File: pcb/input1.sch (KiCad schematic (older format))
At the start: 32 parts, among them Q1 BC847, Q2 BC847, U10 SN74LVCC4245APW, U11 SN74LVCC4245APW, U14 SN74LVCC4245APW, U18 SN74LVCC4245APW, U19 SN74LVCC4245APW, U20 SN74LVC2G17, U4 PCEngineExpansion, U9 SN74LVCC4245APW

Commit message: New layout checkpoint
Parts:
- Q1, Q2: symbol Transistor_BJT:BC847 -> pcehd-rescue:BC847-Transistor_BJT
- R22, R23, R24, R25, R26, R27, R28, R29, R30: symbol Device:R_Small -> pcehd-rescue:R_Small-Device
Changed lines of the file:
@@
 EESchema Schematic File Version 4
-LIBS:pcehd-cache
 EELAYER 30 0
 EELAYER END
@@
 CS_O
 $Comp
-L Device:R_Small R28
+L pcehd-rescue:R_Small-Device R28
 U 1 1 5E20B4F6
 P 2600 6150
@@
 	2700 5950 2700 5500
 $Comp
-L Device:R_Small R27
+L pcehd-rescue:R_Small-Device R27
 U 1 1 5E220BE1
 P 2600 4050
@@
 	2700 2050 2600 2050
 $Comp
-L Device:R_Small R22
+L pcehd-rescue:R_Small-Device R22
 U 1 1 5E4396BE
 P 2600 1950
@@
 $EndComp
 $Comp
-L Device:R_Small R26
+L pcehd-rescue:R_Small-Device R26
 U 1 1 5E1D0EB3
 P 6450 1250
@@
 $EndComp
 $Comp
-L Device:R_Small R29
+L pcehd-rescue:R_Small-Device R29
 U 1 1 610BFA1D
 P 6400 3450
@@
 	10000 5950 10350 5950
 $Comp
-L Transistor_BJT:BC847 Q1
+L pcehd-rescue:BC847-Transistor_BJT Q1
 U 1 1 5F31D333
 P 10250 6200
@@
 $EndComp
 $Comp
-L Device:R_Small R23
+L pcehd-rescue:R_Small-Device R23
 U 1 1 5F31D320
 P 9650 6200
@@
 $EndComp
 $Comp
-L Device:R_Small R30
+L pcehd-rescue:R_Small-Device R30
 U 1 1 5F31D31A
 P 9800 6350
@@
 	9950 4850 10300 4850
 $Comp
-L Transistor_BJT:BC847 Q2
+L pcehd-rescue:BC847-Transistor_BJT Q2
 U 1 1 60FF82DE
 P 10200 5100
@@
 $EndComp
 $Comp
-L Device:R_Small R24
+L pcehd-rescue:R_Small-Device R24
 U 1 1 60C571BE
 P 9600 5100
@@
 $EndComp
 $Comp
-L Device:R_Small R25
+L pcehd-rescue:R_Small-Device R25
 U 1 1 60C54728
 P 9750 5250

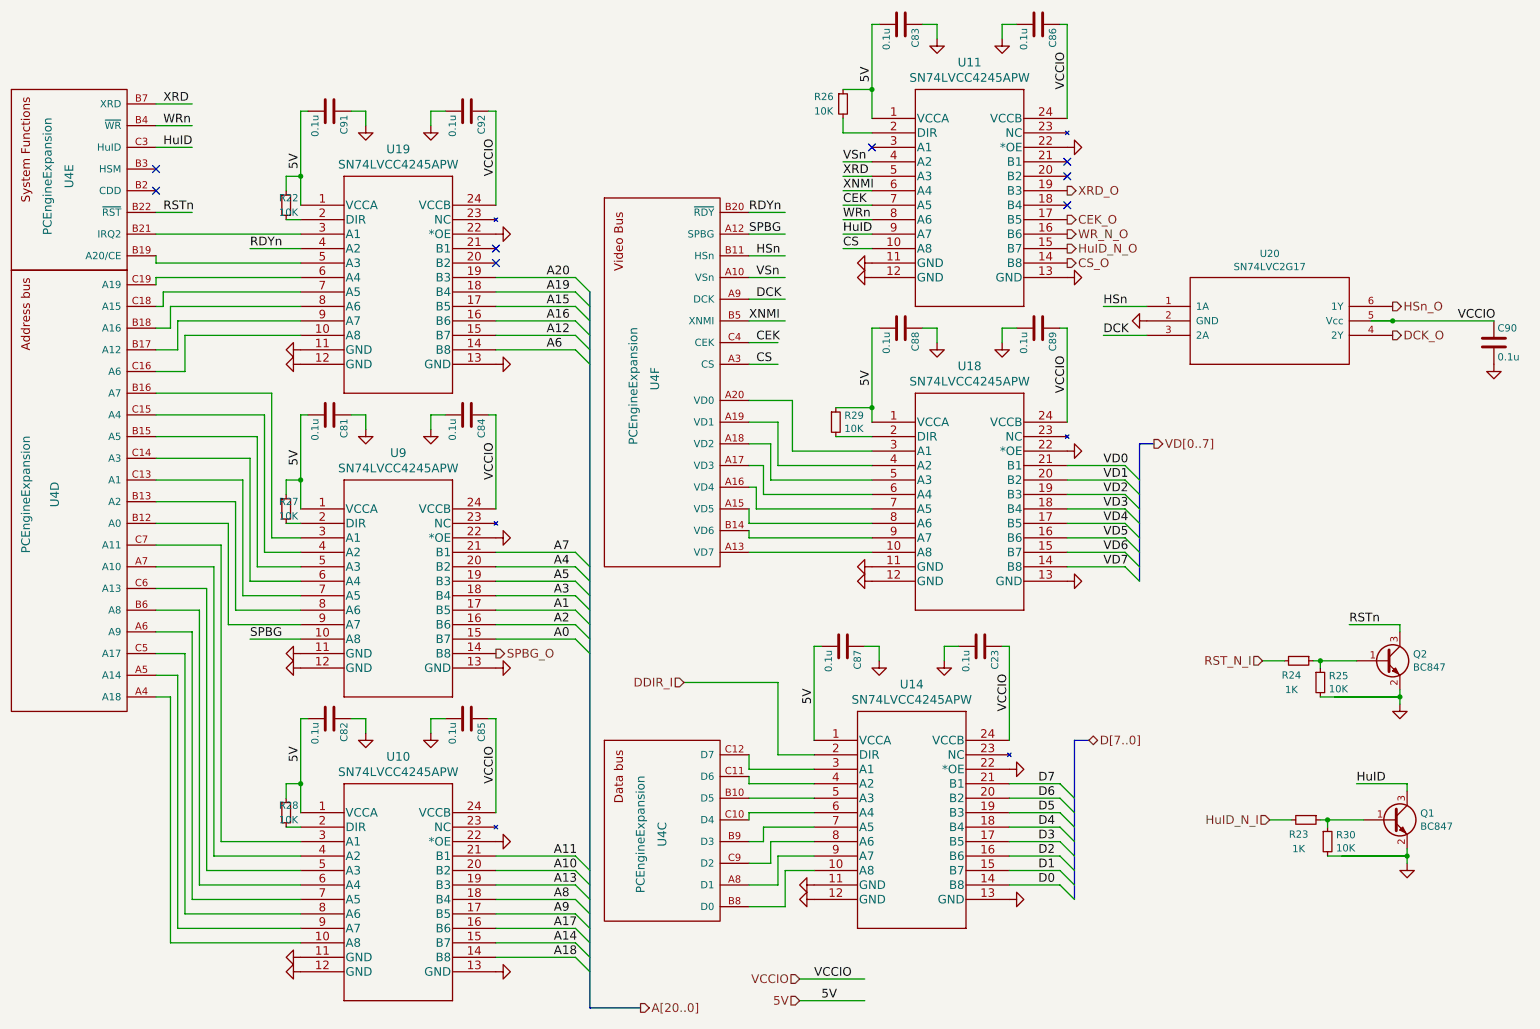
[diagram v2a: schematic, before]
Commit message: Added CDD signal to last open IO pin
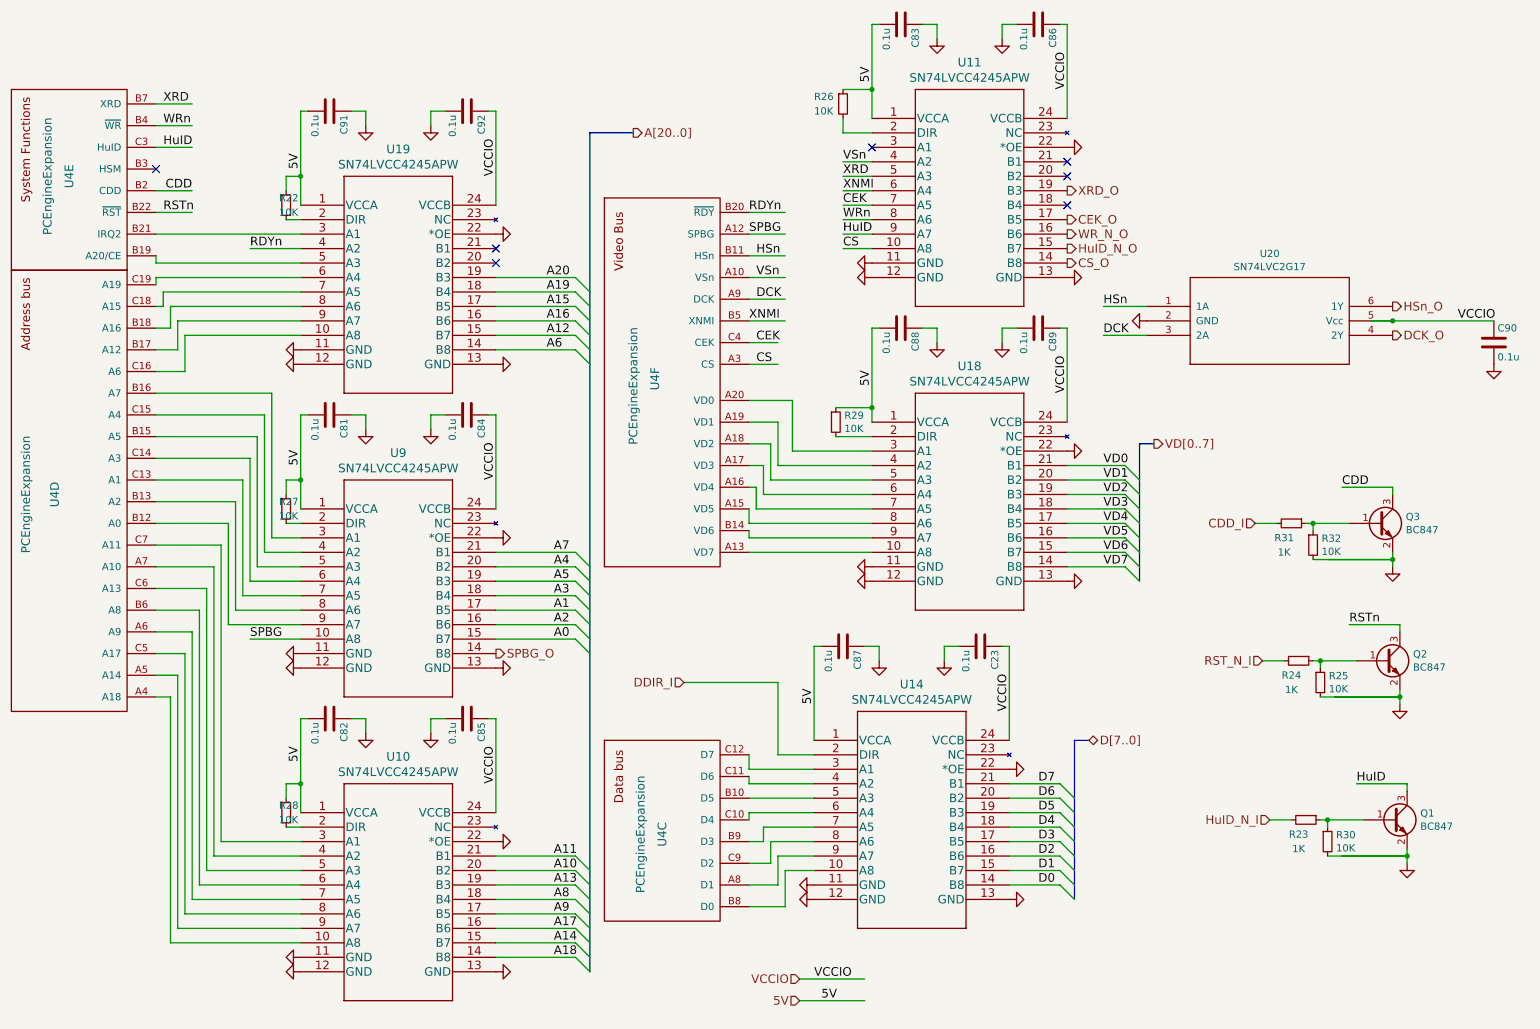
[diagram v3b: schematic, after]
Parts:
- added Q3: BC847, Package_TO_SOT_SMD:SOT-23, symbol pcehd-rescue:BC847-Transistor_BJT
- added R31: 1K, custom_components:SM0603_Resistor_libcms, symbol pcehd-rescue:R_Small-Device
- added R32: 10K, custom_components:SM0603_Resistor_libcms, symbol pcehd-rescue:R_Small-Device
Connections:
- net labels added: CDD, CDD_I
- wire segments 255 -> 266
- no-connect marks 8 -> 7
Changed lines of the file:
@@
 Sheet 5 5
 Title "PCEHD"
-Date "2020-01-12"
+Date "2020-01-18"
 Rev "0.1"
 Comp ""
@@
 WRn
 NoConn ~ 1700 1700
-NoConn ~ 1700 1850
 Wire Wire Line
 	1700 1550 1950 1550
@@
 Entry Wire Line
 	4600 7050 4700 7150
-Text HLabel 5050 7500 2    60   Output ~ 0
+Text HLabel 5000 1450 2    60   Output ~ 0
 A[20..0]
 Text Label 4400 2450 0    60   ~ 0
@@
 Wire Wire Line
 	6000 5250 5350 5250
-Wire Bus Line
-	4700 7500 5050 7500
 Text Label 10000 5950 0    60   ~ 0
 HuID
@@
 Text HLabel 8000 1850 2    60   Output ~ 0
 XRD_O
-NoConn ~ 6650 1550
-NoConn ~ 8000 1650
 Wire Wire Line
 	8550 2650 8250 2650
@@
 Wire Wire Line
 	8550 2850 8250 2850
+Wire Wire Line
+	1700 1850 1950 1850
+NoConn ~ 8000 1650
+NoConn ~ 6650 1550
+Text Label 1950 1850 2    60   ~ 0
+CDD
+Text Label 9900 3900 0    60   ~ 0
+CDD
+Connection ~ 9700 4150
+Wire Wire Line
+	9700 4150 9950 4150
+Wire Wire Line
+	9900 3900 10250 3900
+$Comp
+L pcehd-rescue:BC847-Transistor_BJT Q3
+U 1 1 5E2B9DE0
+P 10150 4150
+F 0 "Q3" H 10341 4196 50  0000 L CNN
+F 1 "BC847" H 10341 4105 50  0000 L CNN
+F 2 "Package_TO_SOT_SMD:SOT-23" H 10350 4075 50  0001 L CIN
+F 3 "http://www.infineon.com/dgdl/Infineon-BC847SERIES_BC848SERIES_BC849SERIES_BC850SERIES-DS-v01_01-en.pdf?fileId=db3a304314dca389011541d4630a1657" H 10150 4150 50  0001 L CNN
+	1    10150 4150
+	1    0    0    -1
+$EndComp
+Connection ~ 10250 4400
+Wire Wire Line
+	10250 4400 10250 4350
+Wire Wire Line
+	10250 4400 10250 4450
+Wire Wire Line
+	9650 4150 9700 4150
+Wire Wire Line
+	9700 4200 9700 4150
+Wire Wire Line
+	10250 3900 10250 3950
+Wire Wire Line
+	9300 4150 9450 4150
+$Comp
+L pcehd-rescue:GND-power #PWR0180
+U 1 1 5E2B9DED
+P 10250 4450
+F 0 "#PWR0180" H 10250 4450 30  0001 C CNN
+F 1 "GND" H 10250 4380 30  0001 C CNN
+F 2 "" H 10250 4450 60  0001 C CNN
+F 3 "" H 10250 4450 60  0000 C CNN
+	1    10250 4450
+	1    0    0    -1
+$EndComp
+$Comp
+L pcehd-rescue:R_Small-Device R31
+U 1 1 5E2B9DF3
+P 9550 4150
+F 0 "R31" V 9650 4100 50  0000 C CNN
+F 1 "1K" V 9750 4100 50  0000 C CNN
+F 2 "custom_components:SM0603_Resistor_libcms" H 9550 4150 50  0001 C CNN
+F 3 "~" H 9550 4150 50  0001 C CNN
+	1    9550 4150
+	0    1    1    0
+$EndComp
+$Comp
+L pcehd-rescue:R_Small-Device R32
+U 1 1 5E2B9DF9
+P 9700 4300
+F 0 "R32" H 9759 4346 50  0000 L CNN
+F 1 "10K" H 9759 4255 50  0000 L CNN
+F 2 "custom_components:SM0603_Resistor_libcms" H 9700 4300 50  0001 C CNN
+F 3 "~" H 9700 4300 50  0001 C CNN
+	1    9700 4300
+	1    0    0    -1
+$EndComp
+Text HLabel 9300 4150 0    60   Input ~ 0
+CDD_I
+Wire Wire Line
+	9800 4400 10250 4400
+Wire Wire Line
+	9700 4400 10250 4400
+Wire Bus Line
+	4700 1450 5000 1450
 Wire Bus Line
 	8500 3600 8500 4550
@@
 	8050 5650 8050 6750
 Wire Bus Line
-	4700 2550 4700 7500
+	4700 1450 4700 7250
 $EndSCHEMATC
